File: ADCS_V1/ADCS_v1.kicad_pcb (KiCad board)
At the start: 4 copper layers, 87.6 x 90 mm, 102 parts, among them IC1 Raspberry_Pi_Zero_W__v1.3_, J1 M50-3900842, J2 M50-3902042, U1 PCA9548AD_118, U10 STSPIN250, U2 LIS3MDLTR, U3 LIS3MDLTR, U4 LIS3MDLTR, U5 LIS331DLHTR, U6 LIS331DLHTR, U7 LIS331DLHTR, U8 STSPIN250, U9 STSPIN250

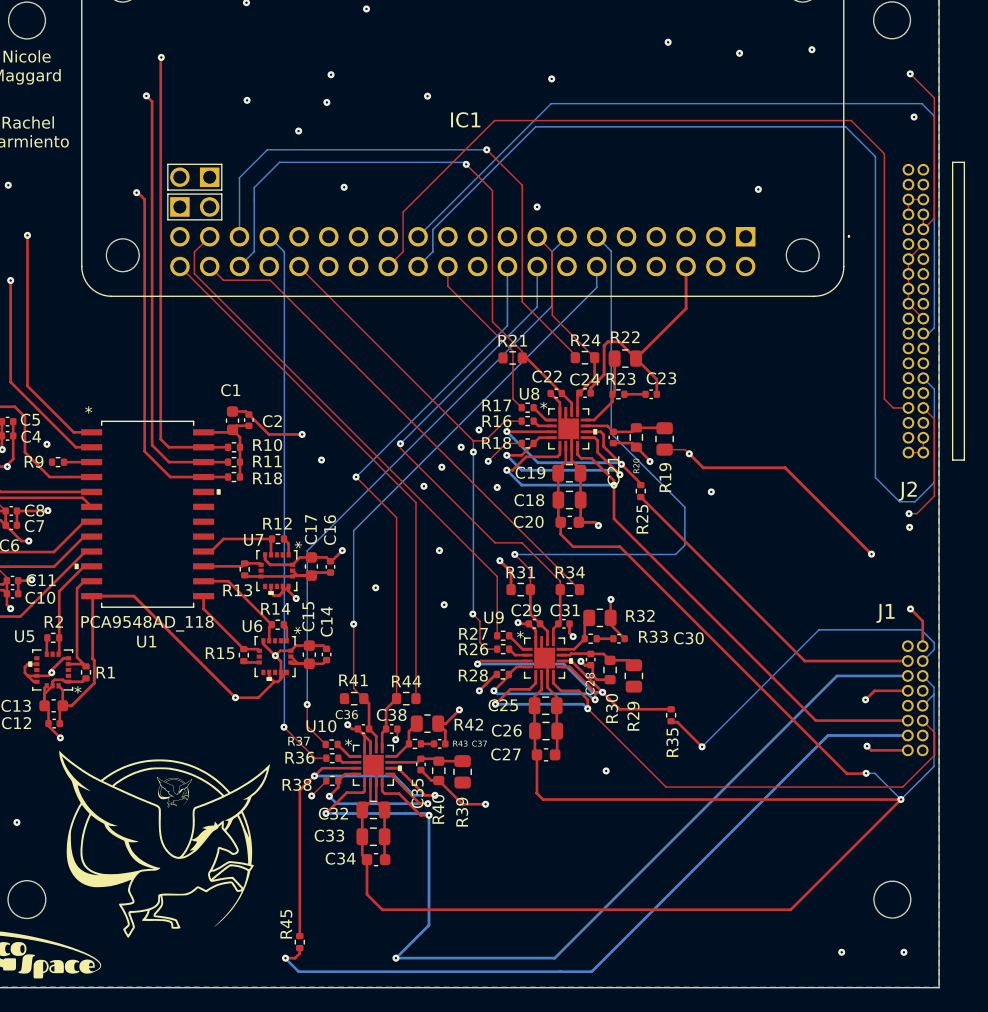
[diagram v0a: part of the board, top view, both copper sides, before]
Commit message: 40 pin and 16 pin def update
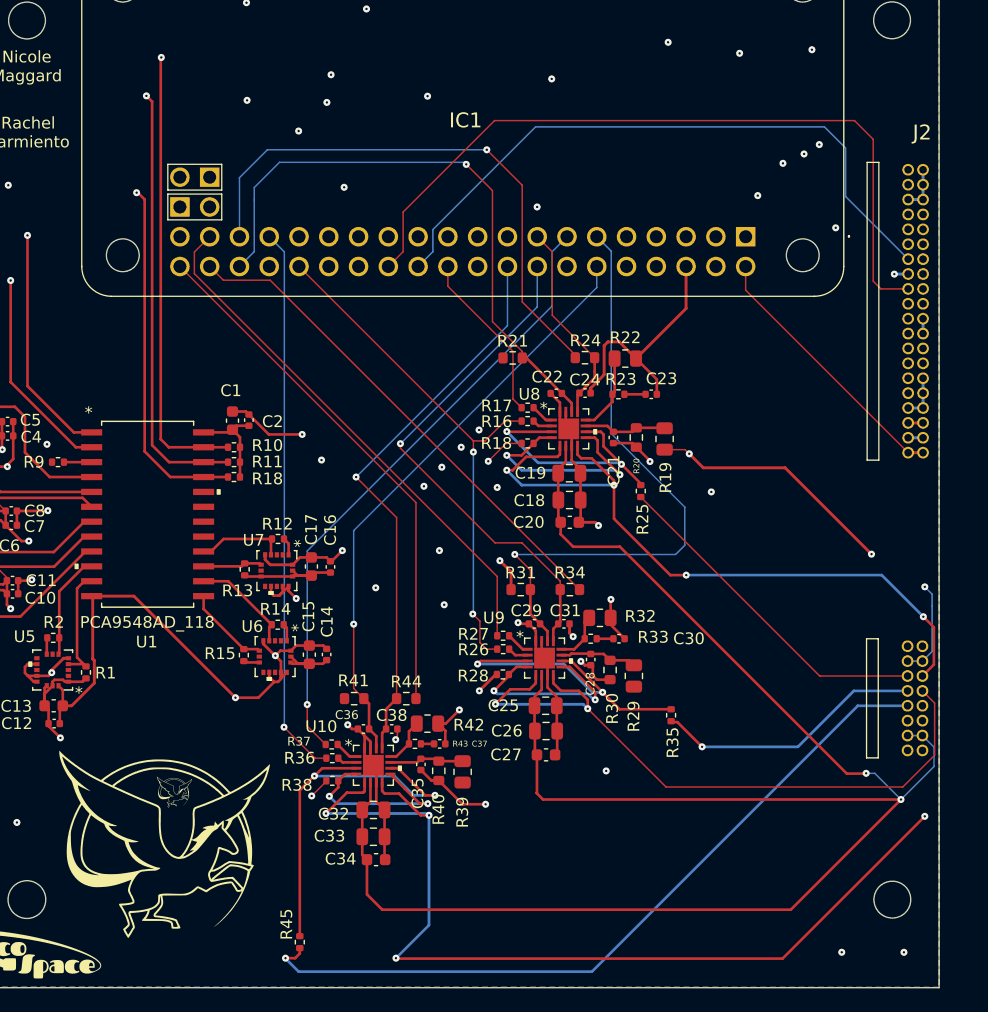
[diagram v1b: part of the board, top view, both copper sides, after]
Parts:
- J1: moved to F.Cu
- moved J2 24.2 mm to (107.8, 36.2), turned to -90 degrees
- moved J1 1.25 mm to (107.8, 76.8)
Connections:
- IC1 pad 26: GPIO11 -> GPIO1
- J1 pad 10: VBAT -> /MAG_Z-
- J1 pad 11: /MAG_X- -> unconnected-(J1-Pad11)
- J1 pad 12: /MAG_Y- -> unconnected-(J1-Pad12)
- J1 pad 13: /MAG_Z+ -> VBAT
- J1 pad 14: unconnected-(J1-Pad14) -> VBAT
- J1 pad 15: GND -> unconnected-(J1-Pad15)
- J1 pad 2: GND -> unconnected-(J1-Pad2)
- J1 pad 3: /MAG_X+ -> GND
- J1 pad 4: /MAG_Y+ -> GND
- J1 pad 5: /MAG_Z+ -> /MAG_X-
- J1 pad 6: VBAT -> /MAG_X+
- J1 pad 7: GND -> /MAG_Y-
- J1 pad 8: unconnected-(J1-Pad8) -> /MAG_Y+
- J1 pad 9: unconnected-(J1-Pad9) -> /MAG_Z-
- J2 pad 10: GND -> SPIO_MOSI
- J2 pad 12: SPIO_CS -> SPIO_MISO
- J2 pad 14: SPIO_MISO -> SPIO_CS
- J2 pad 16: SPIO_MOSI -> GND
- J2 pad 18: SPIO_SCK -> GPIO1
- J2 pad 2: GND -> UART1_RX
- J2 pad 20: GND -> unconnected-(J2-Pad20)
- J2 pad 25: GND -> unconnected-(J2-Pad25)
- J2 pad 27: GND -> unconnected-(J2-Pad27)
- J2 pad 29: unconnected-(J2-Pad29) -> GND
- J2 pad 3: unconnected-(J2-Pad3) -> GND
- J2 pad 30: GND -> unconnected-(J2-Pad30)
- J2 pad 31: unconnected-(J2-Pad31) -> GND
- J2 pad 32: 3.3V -> unconnected-(J2-Pad32)
- J2 pad 34: 3.3V -> GND
- J2 pad 35: GND -> 3.3V
- J2 pad 36: GND -> 3.3V
- J2 pad 37: unconnected-(J2-Pad37) -> GND
- J2 pad 38: 5V -> GND
- J2 pad 39: unconnected-(J2-Pad39) -> 5V
- J2 pad 4: GND -> UART1_TX
- J2 pad 5: unconnected-(J2-Pad5) -> GND
- J2 pad 6: UART1_TX -> GND
- J2 pad 7: GPIO11 -> unconnected-(J2-Pad7)
- J2 pad 8: UART1_RX -> SPIO_SCK
- U10 pad 5: /MAG_Z+ -> /MAG_Z-
- U10 pad 8: /MAG_Z+ -> /MAG_Z-
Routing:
- net /MAG_Z-: track 0.00 -> 9140.0 mm, vias 0 -> 6
- net /MAG_Z+: track 9132.4 -> 0.00 mm, vias 5 -> 0
- net GPIO11: track 73.9 -> 0.00 mm
- net GPIO1: track 0.00 -> 64.5 mm
- net UART1_TX: track 68.8 -> 26.7 mm, vias 1 -> 0
- net UART1_RX: track 70.6 -> 30.1 mm, vias 1 -> 0
- net SPIO_CS: track 89.3 -> 54.9 mm
- net SPIO_MISO: track 67.1 -> 45.4 mm, vias 0 -> 1
- net SPIO_SCK: track 68.4 -> 47.6 mm, vias 0 -> 1
- net SPIO_MOSI: track 62.5 -> 42.3 mm, vias 1 -> 2
- net GND: track 275.6 -> 286.0 mm, vias 49 -> 48
- net /MAG_Y+: track 30.0 -> 23.1 mm
- net VBAT: track 160.5 -> 155.3 mm
- net /MAG_X-: track 55.7 -> 59.2 mm, vias 2 -> 4
- net /MAG_Y-: track 54.7 -> 57.3 mm
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
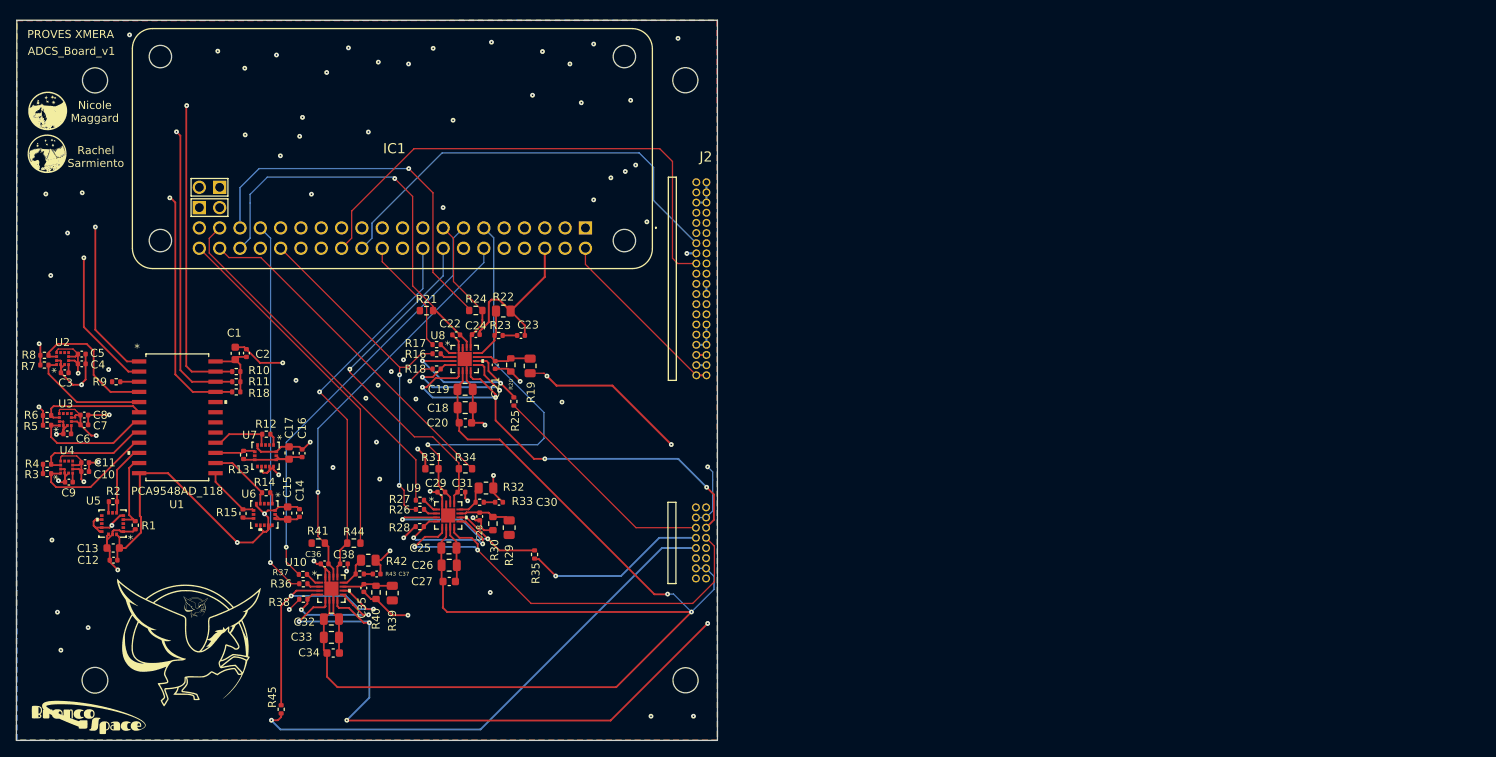
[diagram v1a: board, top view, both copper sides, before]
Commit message: changed connector positions
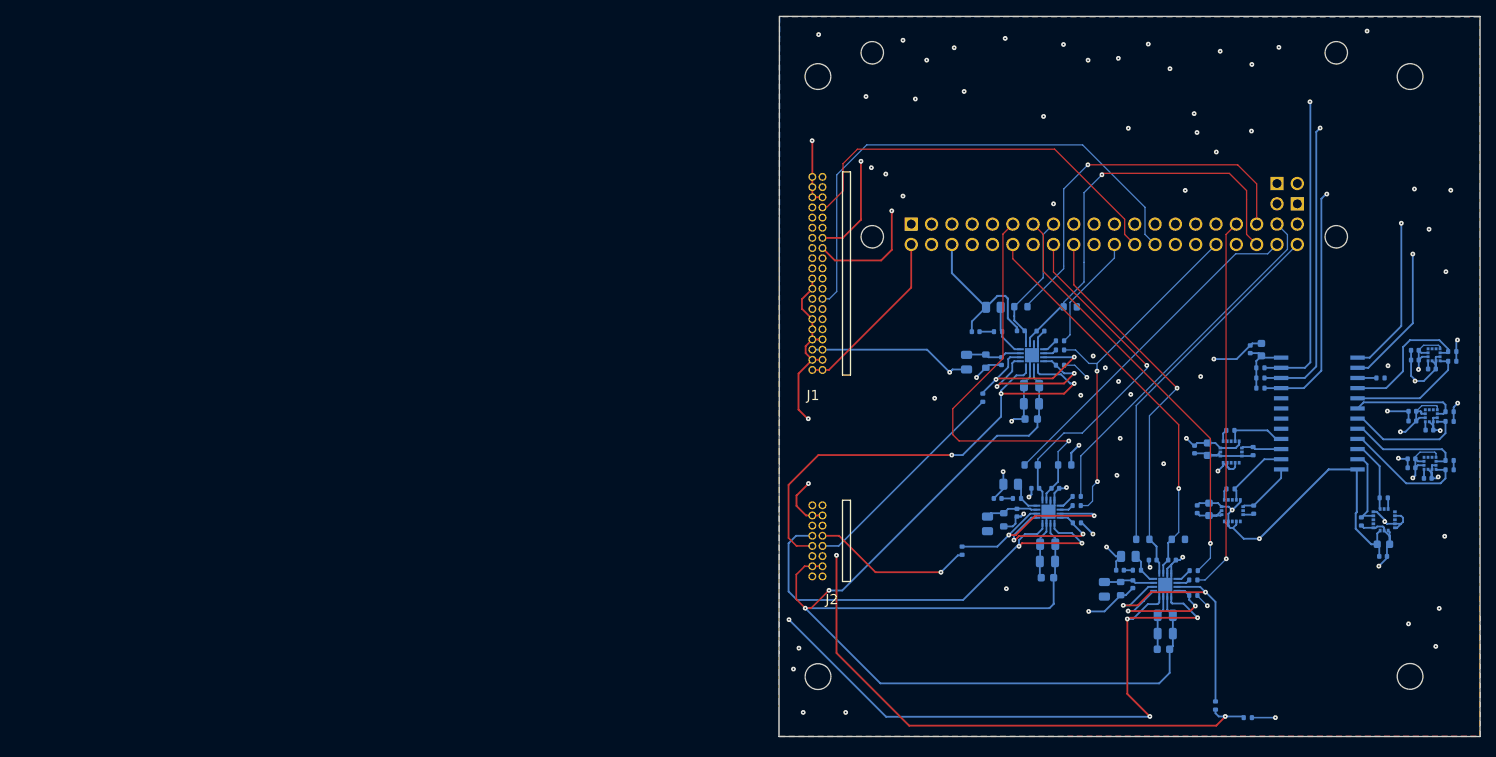
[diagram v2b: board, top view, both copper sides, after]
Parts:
- added R46: 0, Resistor_SMD:R_0402_1005Metric, B.Cu at (175.5, 103.1)
- C1, C18, C2, C28, C38, G*** (x5), IC1, R1, R10, R11, R12, R13, R14, R15, R16, R18, R2, R3, R4, R5, R6, R7, R8, R9, U1, U10, U2, U3, U4, U5, U6, U7, U8, U9: moved to B.Cu
- C10: renamed from C7; moved to B.Cu
- C11: renamed from C10; moved to B.Cu
- C12: renamed from C3; moved to B.Cu
- C13: renamed from C6; moved to B.Cu
- C14: renamed from C9; moved to B.Cu
- C15: renamed from C5; moved to B.Cu
- C16: renamed from C8; moved to B.Cu
- C17: renamed from C11; moved to B.Cu
- C19: renamed from C25; moved to B.Cu
- C20: renamed from C32; moved to B.Cu
- C21: renamed from C19; moved to B.Cu
- C22: renamed from C26; moved to B.Cu
- C23: renamed from C33; moved to B.Cu
- C24: renamed from C20; moved to B.Cu
- C25: renamed from C27; moved to B.Cu
- C26: renamed from C34; moved to B.Cu
- C27: renamed from C21; moved to B.Cu
- C29: renamed from C35; moved to B.Cu
- C3: renamed from C12; moved to B.Cu
- C30: renamed from C22; moved to B.Cu
- C31: renamed from C29; moved to B.Cu
- C32: renamed from C36; moved to B.Cu
- C33: renamed from C23; moved to B.Cu
- C34: renamed from C30; moved to B.Cu
- C35: renamed from C37; moved to B.Cu
- C36: renamed from C24; moved to B.Cu
- C37: renamed from C31; moved to B.Cu
- C4: renamed from C14; moved to B.Cu
- C5: renamed from C16; moved to B.Cu
- C6: renamed from C13; moved to B.Cu
- C7: renamed from C15; moved to B.Cu
- C8: renamed from C17; moved to B.Cu
- C9: renamed from C4; moved to B.Cu
- R17: renamed from R26; moved to B.Cu
- R18: renamed from R36; moved to B.Cu
- R19: renamed from R17; moved to B.Cu
- R20: renamed from R27; moved to B.Cu
- R21: renamed from R37; moved to B.Cu
- R22: renamed from R18; moved to B.Cu
- R23: renamed from R28; moved to B.Cu
- R24: renamed from R38; moved to B.Cu
- R25: renamed from R19; moved to B.Cu
- R26: renamed from R20; moved to B.Cu
- R27: renamed from R21; moved to B.Cu
- R28: renamed from R29; moved to B.Cu
- R29: renamed from R30; moved to B.Cu
- R30: renamed from R39; moved to B.Cu
- R31: renamed from R40; moved to B.Cu
- R32: renamed from R31; moved to B.Cu
- R33: renamed from R41; moved to B.Cu
- R34: renamed from R22; moved to B.Cu
- R35: renamed from R32; moved to B.Cu
- R36: renamed from R42; moved to B.Cu
- R37: renamed from R23; moved to B.Cu
- R38: renamed from R33; moved to B.Cu
- R39: renamed from R43; moved to B.Cu
- R40: renamed from R24; moved to B.Cu
- R41: renamed from R34; moved to B.Cu
- R42: renamed from R44; moved to B.Cu
- R43: renamed from R25; moved to B.Cu
- R44: renamed from R45; moved to B.Cu
- R45: renamed from R35; moved to B.Cu
- moved R7 176.0 mm to (201.1, 58.6), turned to 0 degrees
- moved R8 176.0 mm to (201.1, 57.4), turned to 0 degrees
- moved R3 175.3 mm to (200.7, 72.1), turned to 0 degrees
- moved R4 175.3 mm to (200.7, 71.0), turned to 0 degrees
- moved R5 175.3 mm to (200.7, 66.1), turned to 0 degrees
- moved R6 175.3 mm to (200.7, 64.9), turned to 0 degrees
- moved G*** 175.3 mm to (200.7, 32.2), turned to 180 degrees
- moved G*** 175.2 mm to (200.7, 26.8), turned to 180 degrees
- moved U2 171.4 mm to (198.8, 57.8)
- moved C12 170.9 mm to (198.5, 59.5), turned to 180 degrees
- moved U3 170.7 mm to (198.5, 65.4)
- moved U4 170.4 mm to (198.3, 71.3)
- moved C13 170.3 mm to (198.2, 67.2), turned to 180 degrees
- moved C14 169.9 mm to (198.0, 73.2), turned to 180 degrees
- moved C15 166.6 mm to (196.4, 57.2), turned to 0 degrees
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- renumbered J2 to J1, J1 to J2
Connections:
- IC1 pad 26: GPIO1 -> GPIO4
- J1 pad 1: GND -> 5V
- J1 pad 10: SPIO_MOSI -> unconnected-(J1-Pad10)
- J1 pad 11: unconnected-(J2-Pad11) -> GND
- J1 pad 12: SPIO_MISO -> unconnected-(J1-Pad12)
- J1 pad 14: SPIO_CS -> unconnected-(J1-Pad14)
- J1 pad 16: GND -> GPIO4
- J1 pad 17: unconnected-(J2-Pad17) -> GND
- J1 pad 18: GPIO1 -> unconnected-(J1-Pad18)
- J1 pad 19: unconnected-(J2-Pad19) -> GND
- J1 pad 2: UART1_RX -> 5V
- J1 pad 21: GND -> unconnected-(J1-Pad21)
- J1 pad 23: GND -> unconnected-(J1-Pad23)
- J1 pad 26: unconnected-(J2-Pad26) -> GND
- J1 pad 28: unconnected-(J2-Pad28) -> SPIO_SCK
- J1 pad 29: GND -> unconnected-(J1-Pad29)
- J1 pad 30: unconnected-(J2-Pad30) -> SPIO_MOSI
- J1 pad 31: GND -> unconnected-(J1-Pad31)
- J1 pad 32: unconnected-(J2-Pad32) -> SPIO_MISO
- J1 pad 33: GND -> unconnected-(J1-Pad33)
- J1 pad 34: GND -> SPIO_CS
- J1 pad 35: 3.3V -> GND
- J1 pad 36: 3.3V -> GND
- J1 pad 38: GND -> UART1_RX
- J1 pad 39: 5V -> GND
- J1 pad 4: UART1_TX -> GND
- J1 pad 40: 5V -> UART1_TX
- J1 pad 5: GND -> 3.3V
- J1 pad 6: GND -> 3.3V
- J1 pad 7: unconnected-(J2-Pad7) -> GND
- J1 pad 8: SPIO_SCK -> GND
- J1 pad 9: unconnected-(J2-Pad9) -> GND
- J2 pad 10: /MAG_Z- -> /MAG_Y+
- J2 pad 11: unconnected-(J1-Pad11) -> /MAG_Z-
- J2 pad 12: unconnected-(J1-Pad12) -> /MAG_Z+
- J2 pad 13: VBAT -> GND
- J2 pad 14: VBAT -> GND
- J2 pad 3: GND -> VBAT
- J2 pad 4: GND -> VBAT
- J2 pad 5: /MAG_X- -> GND
- J2 pad 6: /MAG_X+ -> 3.3V
- J2 pad 7: /MAG_Y- -> /MAG_X-
- J2 pad 8: /MAG_Y+ -> /MAG_X+
- J2 pad 9: /MAG_Z- -> /MAG_Y-
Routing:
- net /MAG_Z+: track 0.00 -> 73.7 mm, vias 0 -> 2
- net GPIO4: track 0.00 -> 65.2 mm
- net GPIO1: track 64.5 -> 0.00 mm
- net /MAG_Z-: track 9140.0 -> 9075.7 mm
- net GND: track 286.0 -> 313.4 mm, vias 48 -> 51
- net SPIO_CS: track 54.9 -> 50.1 mm
- net /MAG_X-: track 59.2 -> 63.6 mm, vias 4 -> 3
- net SPIO_MISO: track 45.4 -> 42.1 mm
- net SPIO_SCK: track 47.6 -> 50.6 mm
- net SPIO_MOSI: track 42.3 -> 39.4 mm, vias 2 -> 1
- net /MAG_Y+: track 23.1 -> 20.3 mm
- net UART1_TX: track 26.7 -> 24.4 mm
- net 3.3V: track 119.2 -> 121.2 mm
- net /MAG_Y-: track 57.3 -> 59.3 mm
- net /MAG_X+: track 29.1 -> 27.5 mm
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- added copper zone on B.Cu, net 3.3V
- added copper zone on In2.Cu, net 3.3V
- added copper zone on F.Cu, net GND
- added copper zone on In1.Cu, net GND
- removed copper zone on F.Cu, net 3.3V
- removed copper zone on In1.Cu, net 3.3V
- removed copper zone on B.Cu, net GND
- removed copper zone on In2.Cu, net GND
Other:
- outline, holes or cut-outs redrawn
